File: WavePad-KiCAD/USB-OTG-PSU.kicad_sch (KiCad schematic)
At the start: 8 parts, among them J5 USB_C_Receptacle_USB2.0_14P

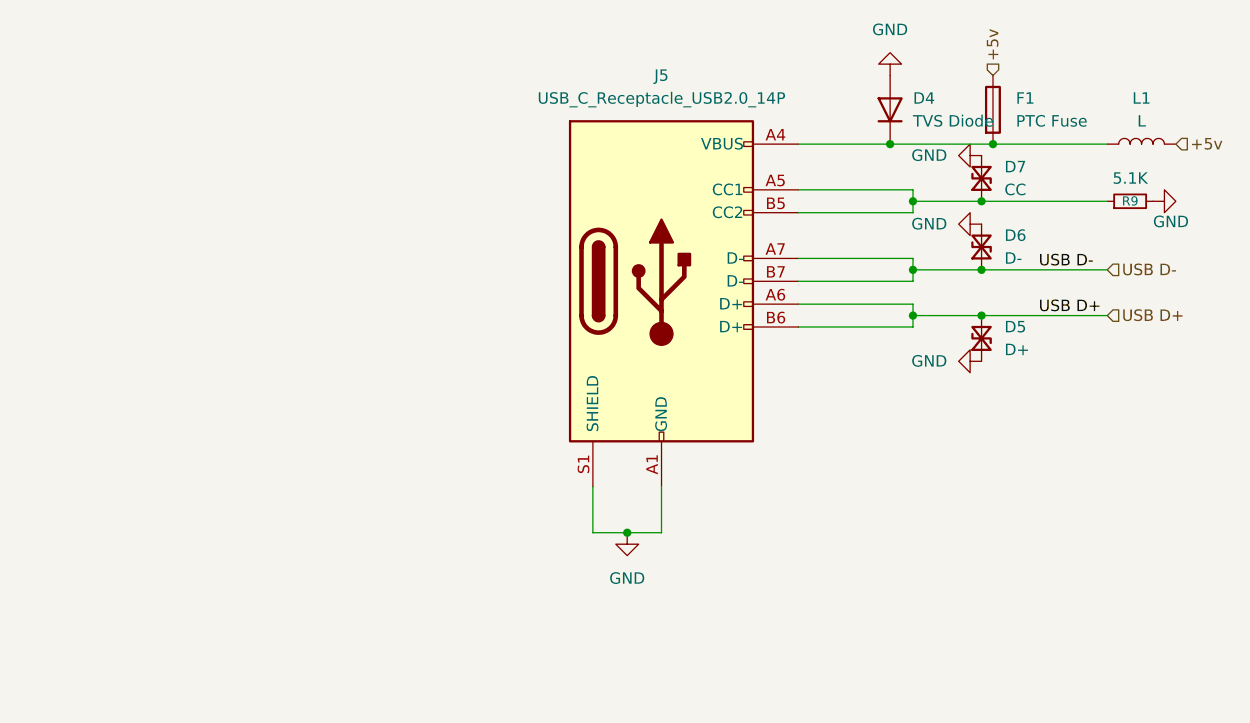
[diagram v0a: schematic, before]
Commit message: Started PCB
Added CSI and DSI connector as well as a USB C with protected  data and Power
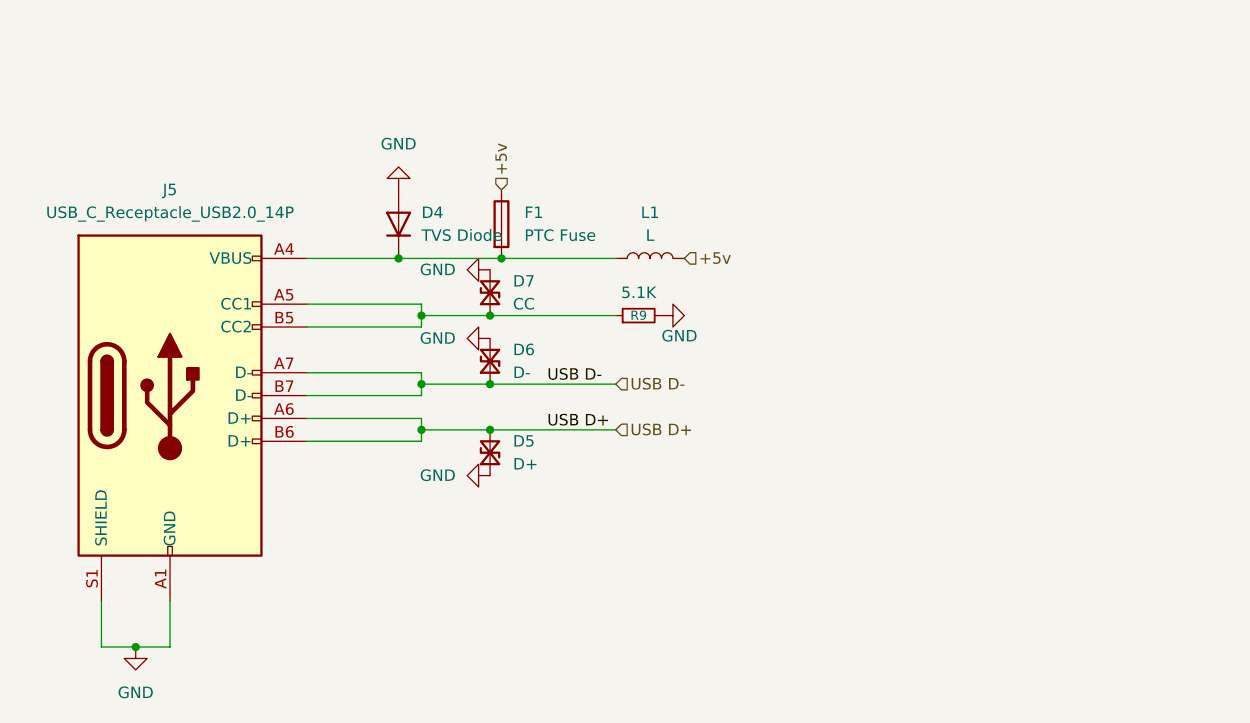
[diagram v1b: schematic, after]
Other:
- title: WavePad CM4 Carrier Board -USB -> (none)
- moved on the sheet: D4, D5, D6, D7, F1, J5, L1, R9
